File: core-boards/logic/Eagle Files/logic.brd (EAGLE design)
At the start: 94.2 x 80.9 mm, 73 parts, among them J1 S3B-VH, J2 B2PS-VH(LF)(SN), J3 B2PS-VH(LF)(SN), J4 B2PS-VH(LF)(SN), J5 B2PS-VH(LF)(SN), J6 B2PS-VH(LF)(SN), J7 B2PS-VH(LF)(SN), J8 B2PS-VH(LF)(SN), Q4 STT4P3LLH6, T1 R-78E5.0-1.0, U1 TC4427ACOA713, U2 TXB0106PWRPW16-M, U3 INA198AIDBVR, U4 TLV70233DBVR, U5 MCP2551T-I/SN, U6 D5V0L1B2WS-7, U7 INA198AIDBVR, X12 B6B-EH-A(LF)(SN), X2 S5B-EH, X3 S5B-EH, X4 B6B-EH-A(LF)(SN), X7 SI-50170, X8 B6B-EH-A(LF)(SN), X9 B6B-EH-A(LF)(SN)

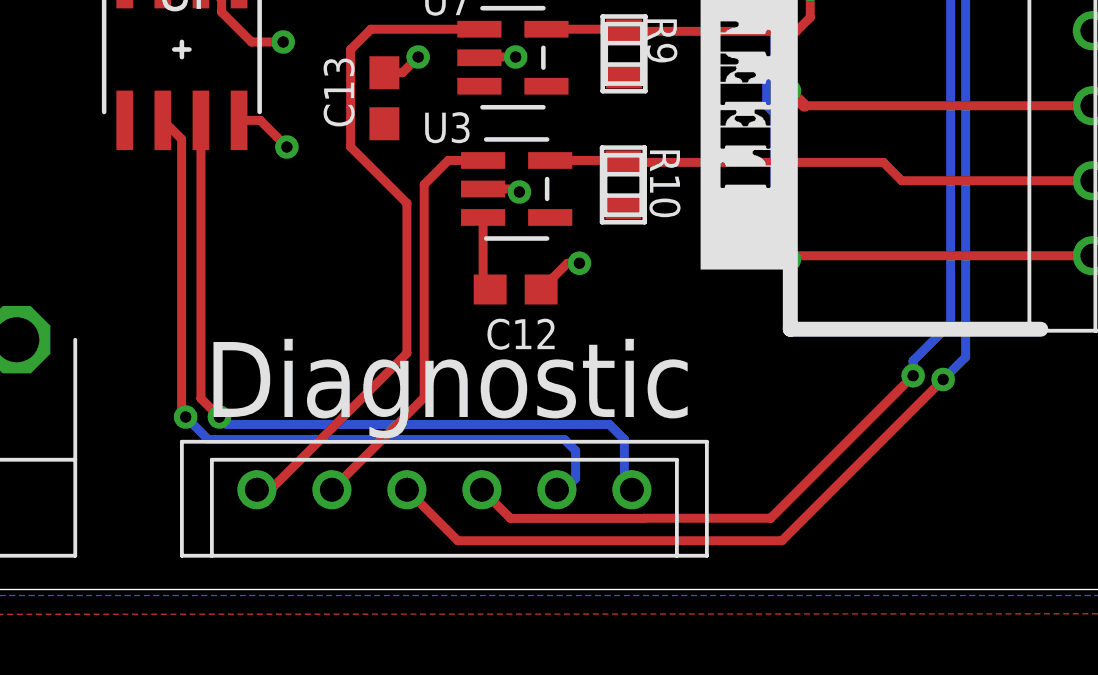
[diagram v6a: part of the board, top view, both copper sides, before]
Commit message: Fixing connector type
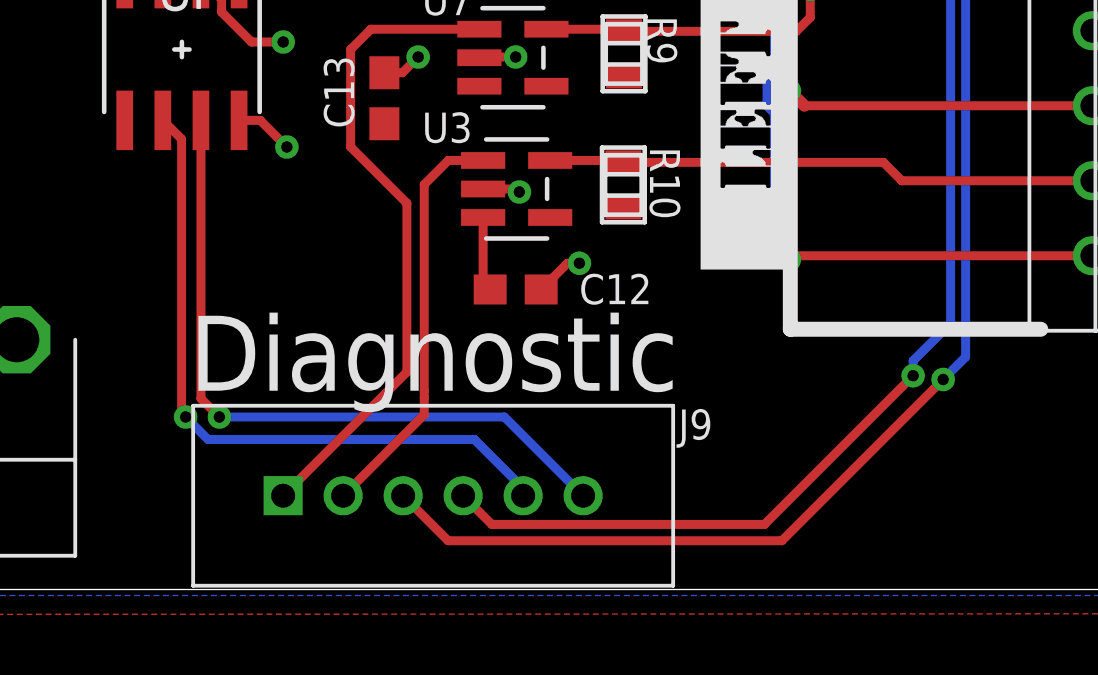
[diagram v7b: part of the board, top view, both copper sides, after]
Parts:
- removed X12: B6B-EH-A(LF)(SN), IGVC-Connector:B6BEHALFSN
- added J9: 6-PIN_2MM-V, RoboJackets-Connectors:2MM-6-V
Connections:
- net CAN_N: now also J9.5; no longer X12.X-5
- net CAN_P: now also J9.6; no longer X12.X-6
- net DIAG_RX: now also J9.4; no longer X12.X-4
- net DIAG_TX: now also J9.3; no longer X12.X-3
- net ENCODER1_SENSE: now also J9.1; no longer X12.X-1
- net ENCODER2_SENSE: now also J9.2; no longer X12.X-2
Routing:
- net CAN_N: track 25.4 -> 22.7 mm
- net CAN_P: track 25.9 -> 23.4 mm
- net DIAG_RX: track 74.1 -> 74.8 mm
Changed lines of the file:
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@@
 <wire x1="21.5" y1="29.625" x2="17.625" y2="29.625" width="0.4" layer="21"/>
 <wire x1="10.7" y1="41.055" x2="10.7" y2="78.255" width="0.5" layer="21"/>
-<text x="57" y="5.75" size="2.5" layer="21" font="vector">Diagnostic</text>
+<text x="56.5" y="6.625" size="2.5" layer="21" font="vector">Diagnostic</text>
 <text x="6" y="36.625" size="2.5" layer="21" font="vector">Lidar #1</text>
 <text x="6" y="17.5" size="2.5" layer="21" font="vector">#2</text>
@@
 <attribute name="MPN" value="B2PS-VH(LF)(SN)" x="8.875" y="45" size="1.778" layer="27" rot="R270" display="off"/>
 </element>
-<element name="X12" library="IGVC-Connector" package="B6BEHALFSN" value="B6B-EH-A(LF)(SN)" x="56.25" y="1.125" smashed="yes"/>
 <element name="U$7" library="MotorBoardDev" package="12V" value="" x="10.63" y="57.9" smashed="yes" rot="R270"/>
 <element name="U7" library="IGVC-Sensor" package="DBV5" value="INA198AIDBVR" x="65.125" y="19.25" smashed="yes">
@@
 </element>
 <element name="C12" library="rcl" library_urn="urn:adsk.eagle:library:334" package="C0603" package3d_urn="urn:adsk.eagle:package:23616/2" value="0.1uF" x="67.375" y="10" smashed="yes">
-<attribute name="NAME" x="66.365" y="8.01" size="1" layer="25" font="vector"/>
+<attribute name="NAME" x="69.49" y="9.51" size="1" layer="25" font="vector"/>
 <attribute name="SPICEPREFIX" value="C" x="67.375" y="10" size="1.778" layer="27" display="off"/>
 </element>
@@
 <attribute name="VALUE" x="11.1478" y="58.74" size="1.27" layer="21" ratio="6" rot="SR0"/>
 <attribute name="VENDOR" value="Diodes Inc" x="12.875" y="59.375" size="1.778" layer="27" display="off"/>
+</element>
+<element name="J9" library="RoboJackets-Connectors" package="2MM-6-V" value="6-PIN_2MM-V" x="63.625" y="3.125" smashed="yes">
+<attribute name="NAME" x="73.375" y="5" size="1" layer="25" font="vector" ratio="10" align="bottom-center"/>
+<attribute name="PINS" value="6" x="63.625" y="3.125" size="1.778" layer="27" display="off"/>
+<attribute name="PIN_PITCH" value="2.0 mm" x="63.625" y="3.125" size="1.778" layer="27" display="off"/>
 </element>
 </elements>
@@
 </signal>
 <signal name="ENCODER1_SENSE">
-<contactref element="X12" pad="X-1"/>
 <contactref element="U7" pad="1"/>
 <wire x1="62.551" y1="18.676" x2="61.875" y2="18" width="0.3" layer="1"/>
 <wire x1="61.875" y1="18" x2="61.875" y2="14.75" width="0.3" layer="1"/>
-<wire x1="63.75" y1="12.875" x2="63.75" y2="7.875" width="0.3" layer="1"/>
 <wire x1="66.1664" y1="18.676" x2="62.551" y2="18.676" width="0.3" layer="1"/>
 <wire x1="61.875" y1="14.75" x2="63.75" y2="12.875" width="0.3" layer="1"/>
-<wire x1="63.75" y1="7.875" x2="59.2" y2="3.325" width="0.3" layer="1"/>
-<wire x1="59.2" y1="3.325" x2="58.75" y2="3.325" width="0.3" layer="1"/>
+<contactref element="J9" pad="1"/>
+<wire x1="63.75" y1="7.25" x2="59.625" y2="3.125" width="0.3" layer="1"/>
+<wire x1="63.75" y1="12.875" x2="63.75" y2="7.25" width="0.3" layer="1"/>
 </signal>
 <signal name="ENCODER2_SENSE">
-<contactref element="X12" pad="X-2"/>
 <contactref element="U3" pad="1"/>
 <wire x1="65.1284" y1="14.301" x2="64.3274" y2="13.5" width="0.3" layer="1"/>
 <wire x1="65.1284" y1="14.301" x2="66.2914" y2="14.301" width="0.3" layer="1"/>
-<wire x1="64.3274" y1="6.4024" x2="61.25" y2="3.325" width="0.3" layer="1"/>
-<wire x1="64.3274" y1="13.5" x2="64.3274" y2="6.4024" width="0.3" layer="1"/>
+<wire x1="64.3274" y1="13.5" x2="64.3274" y2="6.625" width="0.3" layer="1"/>
+<contactref element="J9" pad="2"/>
+<wire x1="64.3274" y1="6.625" x2="64.3274" y2="6.4024" width="0.3" layer="1"/>
+<wire x1="64.3274" y1="6.4024" x2="64.3274" y2="5.8274" width="0.3" layer="1"/>
+<wire x1="64.3274" y1="5.8274" x2="61.625" y2="3.125" width="0.3" layer="1"/>
 </signal>
 <signal name="+5V_ENCODER1">
@@
 <wire x1="81.875" y1="44.75" x2="81.25" y2="45.375" width="0.3" layer="16"/>
 <wire x1="81.875" y1="44.75" x2="81.875" y2="8.875" width="0.3" layer="16"/>
-<contactref element="X12" pad="X-4"/>
 <wire x1="80.625" y1="7.625" x2="80.625" y2="7.125" width="0.3" layer="16"/>
 <via x="80.625" y="7.125" extent="1-16" drill="0.381"/>
-<wire x1="80.625" y1="7.125" x2="75.875" y2="2.375" width="0.3" layer="1"/>
-<wire x1="71.65255625" y1="2.375" x2="71.64615625" y2="2.3686" width="0.3" layer="1"/>
-<wire x1="71.64615625" y1="2.3686" x2="67.2064" y2="2.3686" width="0.3" layer="1"/>
-<wire x1="67.2064" y1="2.3686" x2="66.25" y2="3.325" width="0.3" layer="1"/>
 <wire x1="81.875" y1="8.875" x2="80.625" y2="7.625" width="0.3" layer="16"/>
-<wire x1="75.875" y1="2.375" x2="71.65255625" y2="2.375" width="0.3" layer="1"/>
 <contactref element="A1" pad="28"/>
 <via x="81.25" y="45.375" extent="1-16" drill="0.381"/>
@@
 <wire x1="72.875" y1="45.5" x2="69.995" y2="48.38" width="0.25" layer="16"/>
 <wire x1="69.995" y1="48.38" x2="64.185" y2="48.38" width="0.25" layer="16"/>
+<contactref element="J9" pad="4"/>
+<wire x1="75.6686" y1="2.1686" x2="66.5814" y2="2.1686" width="0.3" layer="1"/>
+<wire x1="66.5814" y1="2.1686" x2="65.625" y2="3.125" width="0.3" layer="1"/>
+<wire x1="80.625" y1="7.125" x2="75.6686" y2="2.1686" width="0.3" layer="1"/>
 </signal>
 <signal name="DIAG_TX">
@@
 <wire x1="82.375" y1="7.75" x2="81.625" y2="7" width="0.3" layer="16"/>
 <via x="81.625" y="7" extent="1-16" drill="0.381"/>
-<contactref element="X12" pad="X-3"/>
-<wire x1="63.75" y1="3.325" x2="65.45" y2="1.625" width="0.3" layer="1"/>
 <wire x1="76.25" y1="1.625" x2="81.625" y2="7" width="0.3" layer="1"/>
-<wire x1="65.45" y1="1.625" x2="76.25" y2="1.625" width="0.3" layer="1"/>
 <contactref element="A1" pad="27"/>
 <wire x1="81.495" y1="48.38" x2="74.255" y2="48.38" width="0.25" layer="1"/>
 <wire x1="71.715" y1="45.84" x2="64.185" y2="45.84" width="0.25" layer="1"/>
 <wire x1="74.255" y1="48.38" x2="71.715" y2="45.84" width="0.25" layer="1"/>
+<contactref element="J9" pad="3"/>
+<wire x1="63.625" y1="3.125" x2="65.125" y2="1.625" width="0.3" layer="1"/>
+<wire x1="65.125" y1="1.625" x2="76.25" y2="1.625" width="0.3" layer="1"/>
 </signal>
 <signal name="MBED_CAN_RD">
@@
 <signal name="CAN_P">
 <contactref element="U5" pad="7"/>
-<contactref element="X12" pad="X-6"/>
 <wire x1="56.885" y1="15.6378" x2="56.885" y2="6.365" width="0.3" layer="1"/>
 <wire x1="56.885" y1="6.365" x2="57.5" y2="5.75" width="0.3" layer="1"/>
 <via x="57.5" y="5.75" extent="1-16" drill="0.381"/>
-<wire x1="71.25" y1="3.325" x2="71" y2="3.325" width="0.3" layer="16"/>
-<wire x1="70.5" y1="5.5" x2="71" y2="5" width="0.3" layer="16"/>
-<wire x1="70.5" y1="5.5" x2="57.75" y2="5.5" width="0.3" layer="16"/>
-<wire x1="57.5" y1="5.75" x2="57.75" y2="5.5" width="0.3" layer="16"/>
-<wire x1="71" y1="5" x2="71" y2="3.325" width="0.3" layer="16"/>
+<contactref element="J9" pad="6"/>
+<wire x1="57.5" y1="5.75" x2="67" y2="5.75" width="0.3" layer="16"/>
+<wire x1="67" y1="5.75" x2="69.625" y2="3.125" width="0.3" layer="16"/>
 </signal>
 <signal name="CAN_N">
 <contactref element="U5" pad="6"/>
-<contactref element="X12" pad="X-5"/>
 <wire x1="55.615" y1="15.6378" x2="56.24" y2="15.0128" width="0.3" layer="1"/>
 <wire x1="56.24" y1="15.0128" x2="56.24" y2="5.885" width="0.3" layer="1"/>
@@
 <via x="56.375" y="5.75" extent="1-16" drill="0.381"/>
 <wire x1="56.375" y1="5.75" x2="57.125" y2="5" width="0.3" layer="16"/>
-<wire x1="69" y1="5" x2="69.375" y2="4.625" width="0.3" layer="16"/>
-<wire x1="57.125" y1="5" x2="69" y2="5" width="0.3" layer="16"/>
-<wire x1="69.375" y1="4.625" x2="69.375" y2="3.7" width="0.3" layer="16"/>
-<wire x1="69.375" y1="3.7" x2="69" y2="3.325" width="0.3" layer="16"/>
-<wire x1="69" y1="3.325" x2="68.75" y2="3.325" width="0.3" layer="16"/>
+<wire x1="57.125" y1="5" x2="66" y2="5" width="0.3" layer="16"/>
+<contactref element="J9" pad="5"/>
+<wire x1="66" y1="5" x2="67.625" y2="3.375" width="0.3" layer="16"/>
+<wire x1="67.625" y1="3.375" x2="67.625" y2="3.125" width="0.3" layer="16"/>
 </signal>
 <signal name="N$1">

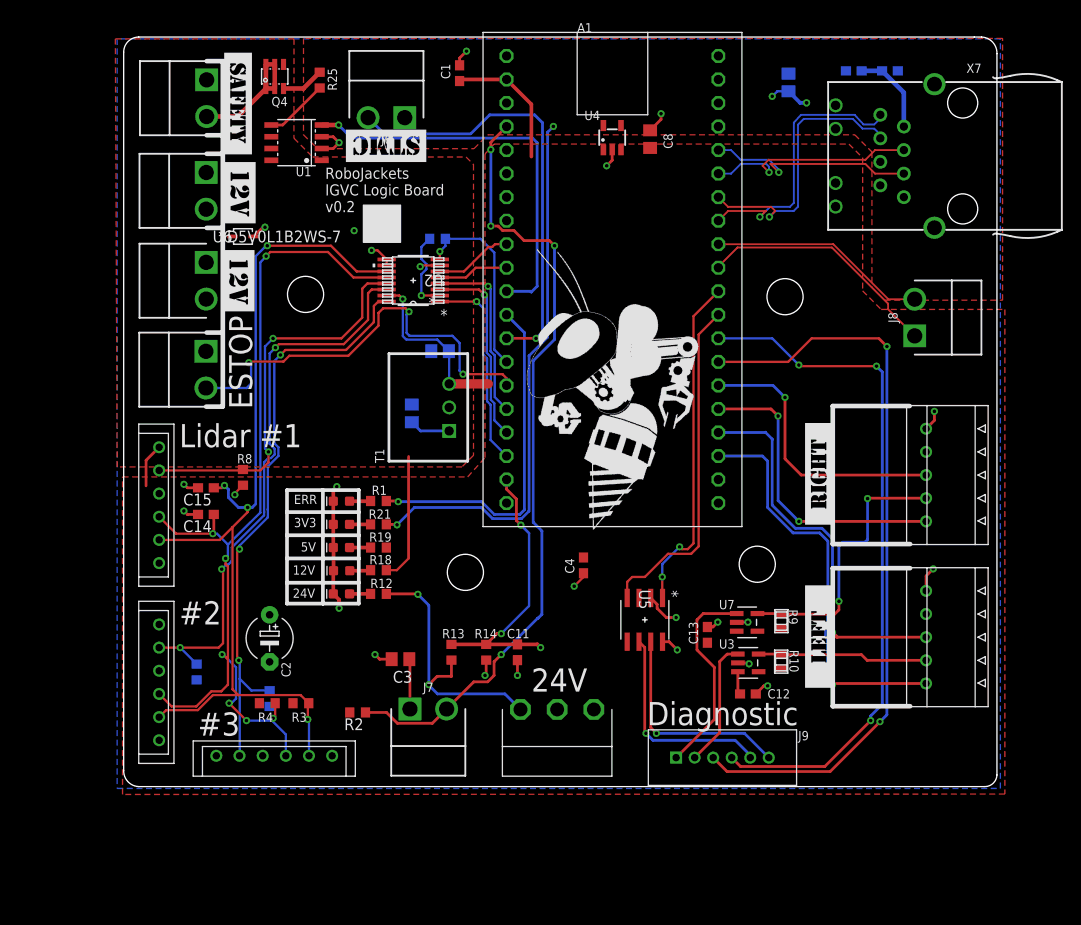
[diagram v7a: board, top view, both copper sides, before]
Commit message: change connector type
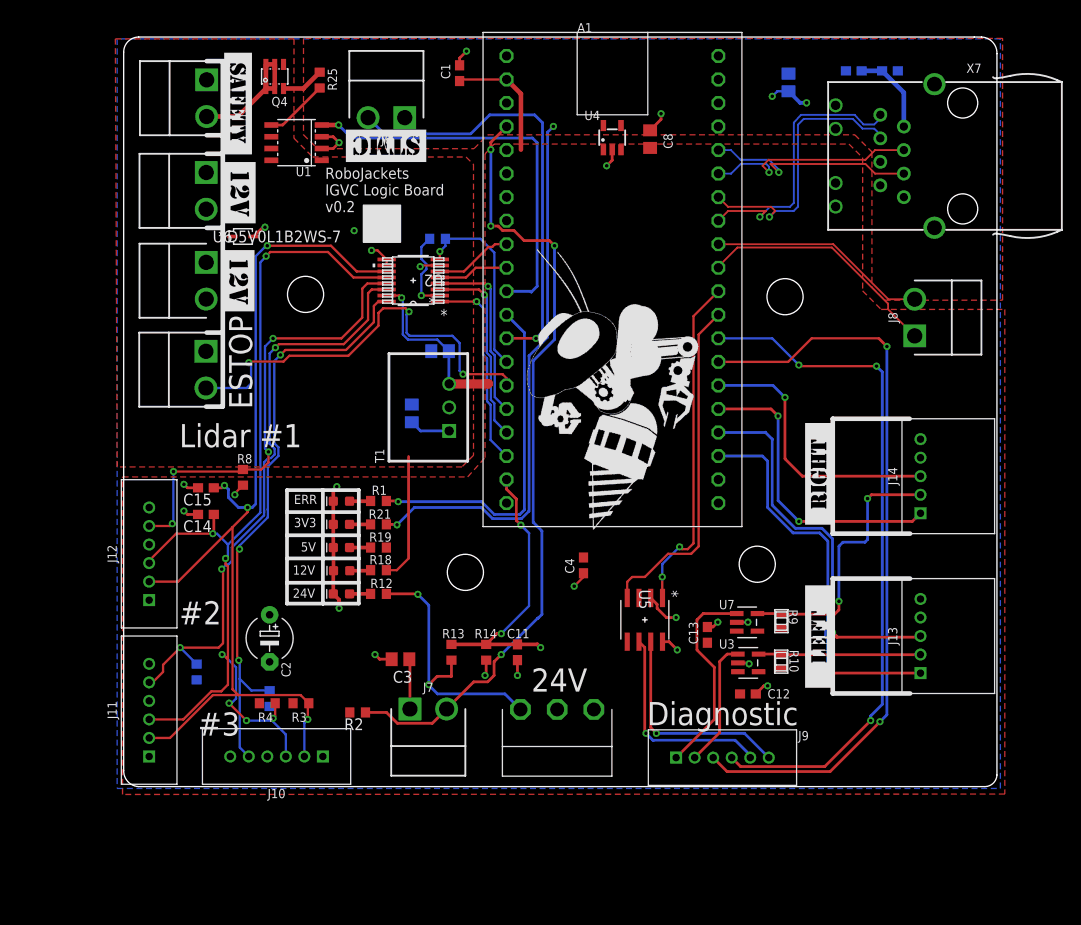
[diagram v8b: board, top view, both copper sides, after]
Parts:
- removed X2, X3: S5B-EH, IGVC-Connector:S5BEHLFSN
- removed X4, X8, X9: B6B-EH-A(LF)(SN), IGVC-Connector:B6BEHALFSN
- added J10, J11, J12: 6-PIN_2MM-V, RoboJackets-Connectors:2MM-6-V
- added J13, J14: 5-PIN_2MM-H, RoboJackets-Connectors:2MM-5-H
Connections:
- net +5V: now also J10.6, J11.6, J12.6; no longer X4.X-1, X8.X-1, X9.X-1
- net +5V_ENCODER1: now also J14.2; no longer X3.X-4
- net +5V_ENCODER2: now also J13.2; no longer X2.X-4
- net GND: now also J10.1, J11.1, J12.1, J13.5, J14.5; no longer X2.X-1, X3.X-1, X4.X-6, X8.X-6, X9.X-6
- net LEA: now also J13.3; no longer X2.X-3
- net LEB: now also J13.1; no longer X2.X-5
- net LIDAR_EN_1_5V: now also J12.5; no longer X4.X-2
- net LIDAR_EN_2_5V: now also J11.5; no longer X8.X-2
- net LIDAR_EN_3_5V: now also J10.5; no longer X9.X-2
- net REA: now also J14.3; no longer X3.X-3
- net REB: now also J14.1; no longer X3.X-5
- net SCL_5V: now also J10.3, J11.3, J12.3; no longer X4.X-4, X8.X-4, X9.X-4
- net SDA_5V: now also J10.2, J11.2, J12.2; no longer X4.X-5, X8.X-5, X9.X-5
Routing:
- net +5V: track 41.1 -> 32.6 mm
- net LIDAR_EN_1_5V: track 42.7 -> 49.4 mm, vias 2 -> 4
- net SDA_5V: track 101.7 -> 106.9 mm
- net GND: track 67.5 -> 62.6 mm, vias 26 -> 24
- net LIDAR_EN_2_5V: track 61.0 -> 64.1 mm
- net SCL_5V: track 101.3 -> 104.3 mm
- net LEB: track 44.6 -> 42.6 mm
- net +5V_ENCODER2: track 18.4 -> 17.5 mm
- net REA: track 30.3 -> 29.8 mm
- net LEA: track 41.7 -> 41.1 mm
